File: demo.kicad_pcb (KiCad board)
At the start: 50 x 30 mm, 3 parts

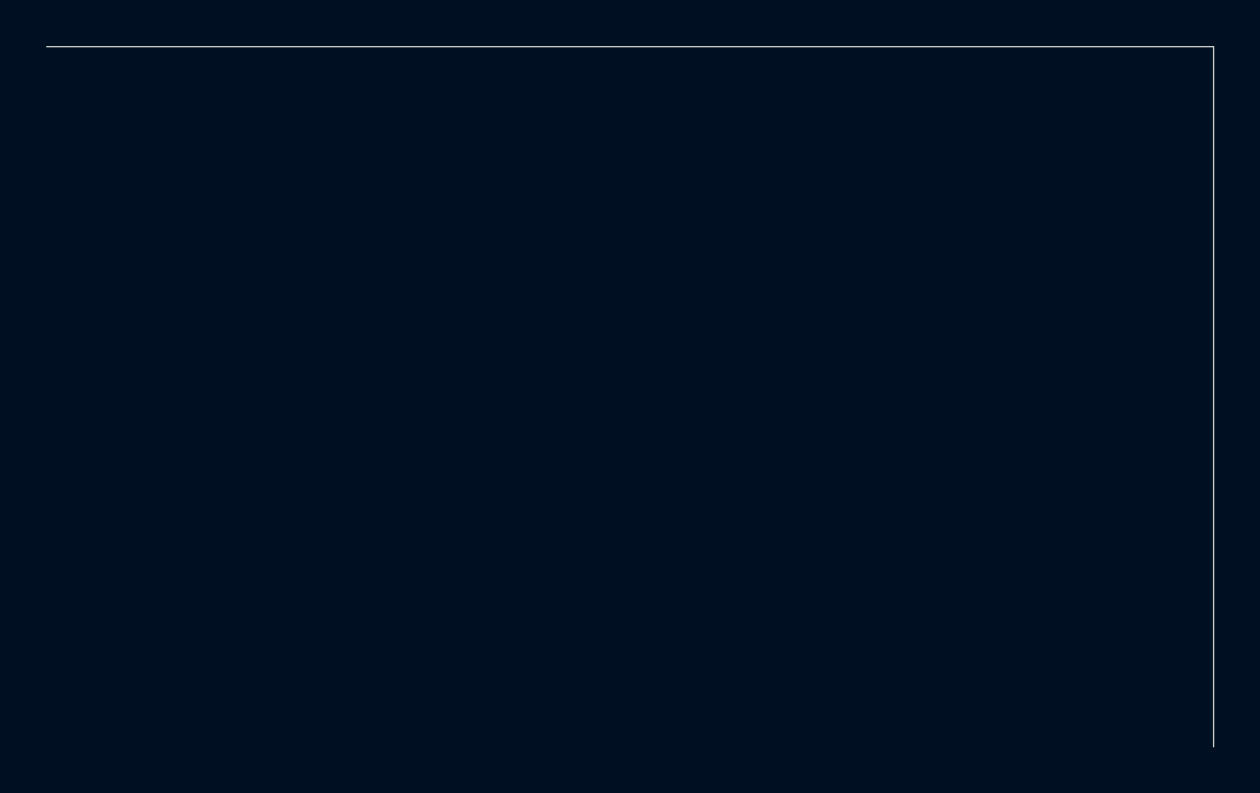
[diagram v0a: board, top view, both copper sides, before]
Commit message: fix: close the outline, deduplicate R2, and source the BOM
Edge.Cuts now describes a closed rectangle, the second resistor is R2 rather than
a second R1, and both BOM lines carry an MPN and a compliance status.

Readiness goes from five findings to none.
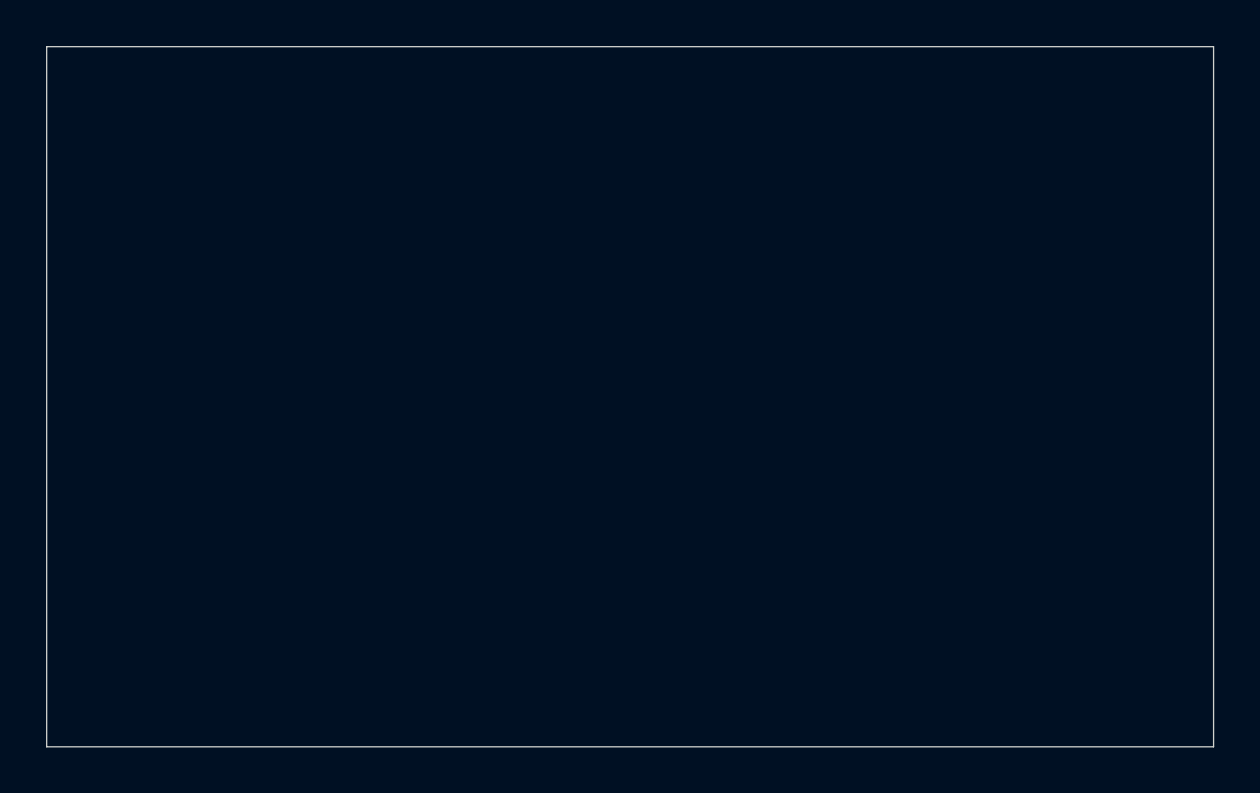
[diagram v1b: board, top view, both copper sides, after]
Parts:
- removed the R1 at (10.0, 5.00)
- added R2: , Resistor_SMD:R_0603, F.Cu at (10.0, 5.00)
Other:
- outline, holes or cut-outs redrawn
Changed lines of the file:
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@@
 (kicad_pcb
   (version 20250114)
-  (gr_line (start 0 0) (end 50 0) (layer "Edge.Cuts"))
-  (gr_line (start 50 0) (end 50 30) (layer "Edge.Cuts"))
+  (title_block (rev "1.0.0"))
+  (gr_rect (start 0 0) (end 50 30) (layer "Edge.Cuts"))
   (footprint "Resistor_SMD:R_0603" (layer "F.Cu") (at 5 5) (property "Reference" "R1"))
-  (footprint "Resistor_SMD:R_0603" (layer "F.Cu") (at 10 5) (property "Reference" "R1"))
+  (footprint "Resistor_SMD:R_0603" (layer "F.Cu") (at 10 5) (property "Reference" "R2"))
   (footprint "Capacitor_SMD:C_0603" (layer "F.Cu") (at 15 5) (property "Reference" "C1"))
 )
